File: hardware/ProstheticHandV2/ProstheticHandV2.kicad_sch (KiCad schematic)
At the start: 35 parts, among them J1 BATT_CONNECTOR, J2 EMG_SENSOR_01, J3 EMG_SENSOR_02, SW1 DIP_SWITCH, U1 LM7805_TO220

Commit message: Update work on schematic
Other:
- removed sheet Sheet2
- removed sheet Sheet3
- added sheet ProstheticHandV2_Sheet2 (ProstheticHandV2_Sheet2.kicad_sch)
- added sheet ProstheticHandV2_Sheet3 (ProstheticHandV2_Sheet3.kicad_sch)
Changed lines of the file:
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@@
+    )
+  )
+  (global_label "POT_01" (shape input) (at 40.64 68.58 180) (fields_autoplaced)
+    (effects (font (size 1.27 1.27)) (justify right))
+    (property "Intersheetrefs" "${INTERSHEET_REFS}" (at 30.7001 68.58 0)
+      (effects (font (size 1.27 1.27)) (justify right) hide)
     )
   )
@@
     )
   )
+  (global_label "BUTTON_01" (shape input) (at 45.72 88.9 180) (fields_autoplaced)
+    (effects (font (size 1.27 1.27)) (justify right))
+    (property "Intersheetrefs" "${INTERSHEET_REFS}" (at 32.1515 88.9 0)
+      (effects (font (size 1.27 1.27)) (justify right) hide)
+    )
+  )
   (global_label "DIP_SWITCH_02" (shape output) (at 43.18 165.1 180) (fields_autoplaced)
     (effects (font (size 1.27 1.27)) (justify right))
@@
     )
   )
+  (global_label "POT_02" (shape input) (at 43.18 73.66 180) (fields_autoplaced)
+    (effects (font (size 1.27 1.27)) (justify right))
+    (property "Intersheetrefs" "${INTERSHEET_REFS}" (at 33.2401 73.66 0)
+      (effects (font (size 1.27 1.27)) (justify right) hide)
+    )
+  )
   (global_label "DIP_SWITCH_03" (shape output) (at 43.18 170.18 180) (fields_autoplaced)
     (effects (font (size 1.27 1.27)) (justify right))
@@
     )
   )
+  (global_label "BUTTON_02" (shape input) (at 43.18 93.98 180) (fields_autoplaced)
+    (effects (font (size 1.27 1.27)) (justify right))
+    (property "Intersheetrefs" "${INTERSHEET_REFS}" (at 29.6115 93.98 0)
+      (effects (font (size 1.27 1.27)) (justify right) hide)
+    )
+  )
   (global_label "DIP_SWITCH_01" (shape input) (at 124.46 71.12 0) (fields_autoplaced)
     (effects (font (size 1.27 1.27)) (justify left))
@@
     (property "Intersheetrefs" "${INTERSHEET_REFS}" (at 141.536 58.42 0)
       (effects (font (size 1.27 1.27)) (justify left) hide)
+    )
+  )
+  (global_label "POT_03" (shape input) (at 43.18 81.28 180) (fields_autoplaced)
+    (effects (font (size 1.27 1.27)) (justify right))
+    (property "Intersheetrefs" "${INTERSHEET_REFS}" (at 33.2401 81.28 0)
+      (effects (font (size 1.27 1.27)) (justify right) hide)
     )
   )
@@
     )
   )
-  (sheet (at 0 457.2) (size 297.18 210.82) (fields_autoplaced)
+  (sheet (at 2.54 228.6) (size 302.26 193.04) (fields_autoplaced)
     (stroke (width 0.1524) (type solid))
     (fill (color 0 0 0 0.0000))
-    (property "Sheetname" "Sheet3" (at 0 456.4884 0)
+    (property "Sheetname" "ProstheticHandV2_Sheet2" (at 2.54 227.8884 0)
       (effects (font (size 1.27 1.27)) (justify left bottom))
     )
-    (property "Sheetfile" "untitled.kicad_sch" (at 0 668.6046 0)
+    (property "Sheetfile" "ProstheticHandV2_Sheet2.kicad_sch" (at 2.54 422.2246 0)
       (effects (font (size 1.27 1.27)) (justify left top))
     )
@@
     )
   )
-  (sheet (at 0 223.52) (size 297.18 210.82) (fields_autoplaced)
+  (sheet (at 5.08 439.42) (size 299.72 180.34) (fields_autoplaced)
     (stroke (width 0.1524) (type solid))
     (fill (color 0 0 0 0.0000))
-    (property "Sheetname" "Sheet2" (at 0 222.8084 0)
+    (property "Sheetname" "ProstheticHandV2_Sheet3" (at 5.08 438.7084 0)
       (effects (font (size 1.27 1.27)) (justify left bottom))
     )
-    (property "Sheetfile" "untitled.kicad_sch" (at 0 434.9246 0)
+    (property "Sheetfile" "ProstheticHandV2_Sheet3.kicad_sch" (at 5.08 620.3446 0)
       (effects (font (size 1.27 1.27)) (justify left top))
     )
     (instances
       (project "ProstheticHandV2"
-        (path "/4b4c4f07-d40b-46d6-800c-cabc6090ace0" (page "2"))
-      )
-    )
+        (path "/4b4c4f07-d40b-46d6-800c-cabc6090ace0" (page "3"))
+      )
+    )

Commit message: Started working on PCB
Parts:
- A1: footprint (none) -> FootprintLibrary:ESP32S3_DevModule
- C1, C2, C5, C6: footprint (none) -> Capacitor_THT:C_Disc_D3.8mm_W2.6mm_P2.50mm
- C3, C4: footprint (none) -> Capacitor_THT:CP_Radial_D8.0mm_P3.50mm
- D1: footprint (none) -> Diode_THT:D_DO-15_P12.70mm_Horizontal
- D2, D3: footprint (none) -> LED_THT:LED_D5.0mm
- D4, D5: footprint (none) -> Diode_THT:D_T-1_P5.08mm_Horizontal
- D6: value GREEN -> LED GREEN; footprint (none) -> LED_THT:LED_D5.0mm
- J1, J2, J3: footprint (none) -> Connector_JST:JST_XA_B02B-XASK-1-A_1x02_P2.50mm_Vertical
- R1, R2, R3, R4, R5, R6, R7, R8, R9: footprint (none) -> Resistor_THT:R_Axial_DIN0207_L6.3mm_D2.5mm_P7.62mm_Horizontal
- SW1: footprint (none) -> Button_Switch_THT:SW_DIP_SPSTx04_Slide_9.78x12.34mm_W7.62mm_P2.54mm
- TP1, TP2, TP3, TP4, TP5, TP6, TP7, TP8: footprint (none) -> TestPoint:TestPoint_Pad_D2.5mm
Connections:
- net +3V3: now also A1.1 (3v3), A1.2 (3v3); no longer A1. (TX)
- net +5V: now also A1.21 (5v); no longer A1. (TX)
- net BATT_SENSE: now also A1.20 (14)
- net BUTTON_01: now also A1.40 (2)
- net BUTTON_02: now also A1.41 (1)
- net DEBUG_LED_01: now also A1.34 (37)
- net DEBUG_LED_02: now also A1.35 (38)
- net DIP_SWITCH_00: now also A1.39 (42)
- net DIP_SWITCH_01: now also A1.38 (41)
- net DIP_SWITCH_02: now also A1.37 (40)
- net DIP_SWITCH_03: now also A1.36 (39)
- net EMG_SENSOR_01: now also A1.10 (17)
- net EMG_SENSOR_02: now also A1.11 (18)
- net GND: now also A1.22 (GND), A1.23 (GND), A1.24 (GND), A1.44 (GND); no longer A1. (TX)
- net POT_01: now also A1.16 (10)
- net POT_02: now also A1.17 (11)
- net POT_03: now also A1.18 (12)
- new net SERVO_CONTROL_01: A1.4
- new net SERVO_CONTROL_02: A1.5
- new net SERVO_CONTROL_03: A1.6
- new net SERVO_CURR_01: A1.7
- new net SERVO_CURR_02: A1.8 (15)
- new net SERVO_CURR_03: A1.9 (16)

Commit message: Finalize PCB design for china
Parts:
- added TP3: TP_GND, TestPoint:TestPoint_Pad_D2.5mm, symbol Connector:TestPoint
- J1, J2, J3: footprint Connector_JST:JST_XA_B02B-XASK-1-A_1x02_P2.50mm_Vertical -> Connector_JST:JST_XA_B02B-XASK-1_1x02_P2.50mm_Vertical
- renumbered C3 to C1, C4 to C3, C1 to C4, D6 to D2, D4 to D3, D5 to D4, D2 to D5, D3 to D6, R9 to R2, R2 to R3, R5 to R4, R6 to R5, R7 to R6, R8 to R7, R3 to R8, R4 to R9, TP5 to TP4, TP7 to TP5, TP8 to TP7, TP3 to TP8, TP4 to TP9
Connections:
- net BUTTON_01: now also A1.41 (1); no longer A1.40 (2)
- net BUTTON_02: now also A1.40 (2); no longer A1.41 (1)
- net EMG_SENSOR_01: now also A1.11 (18); no longer A1.10 (17)
- net EMG_SENSOR_02: now also A1.10 (17); no longer A1.11 (18)
- net GND: now also TP3.1

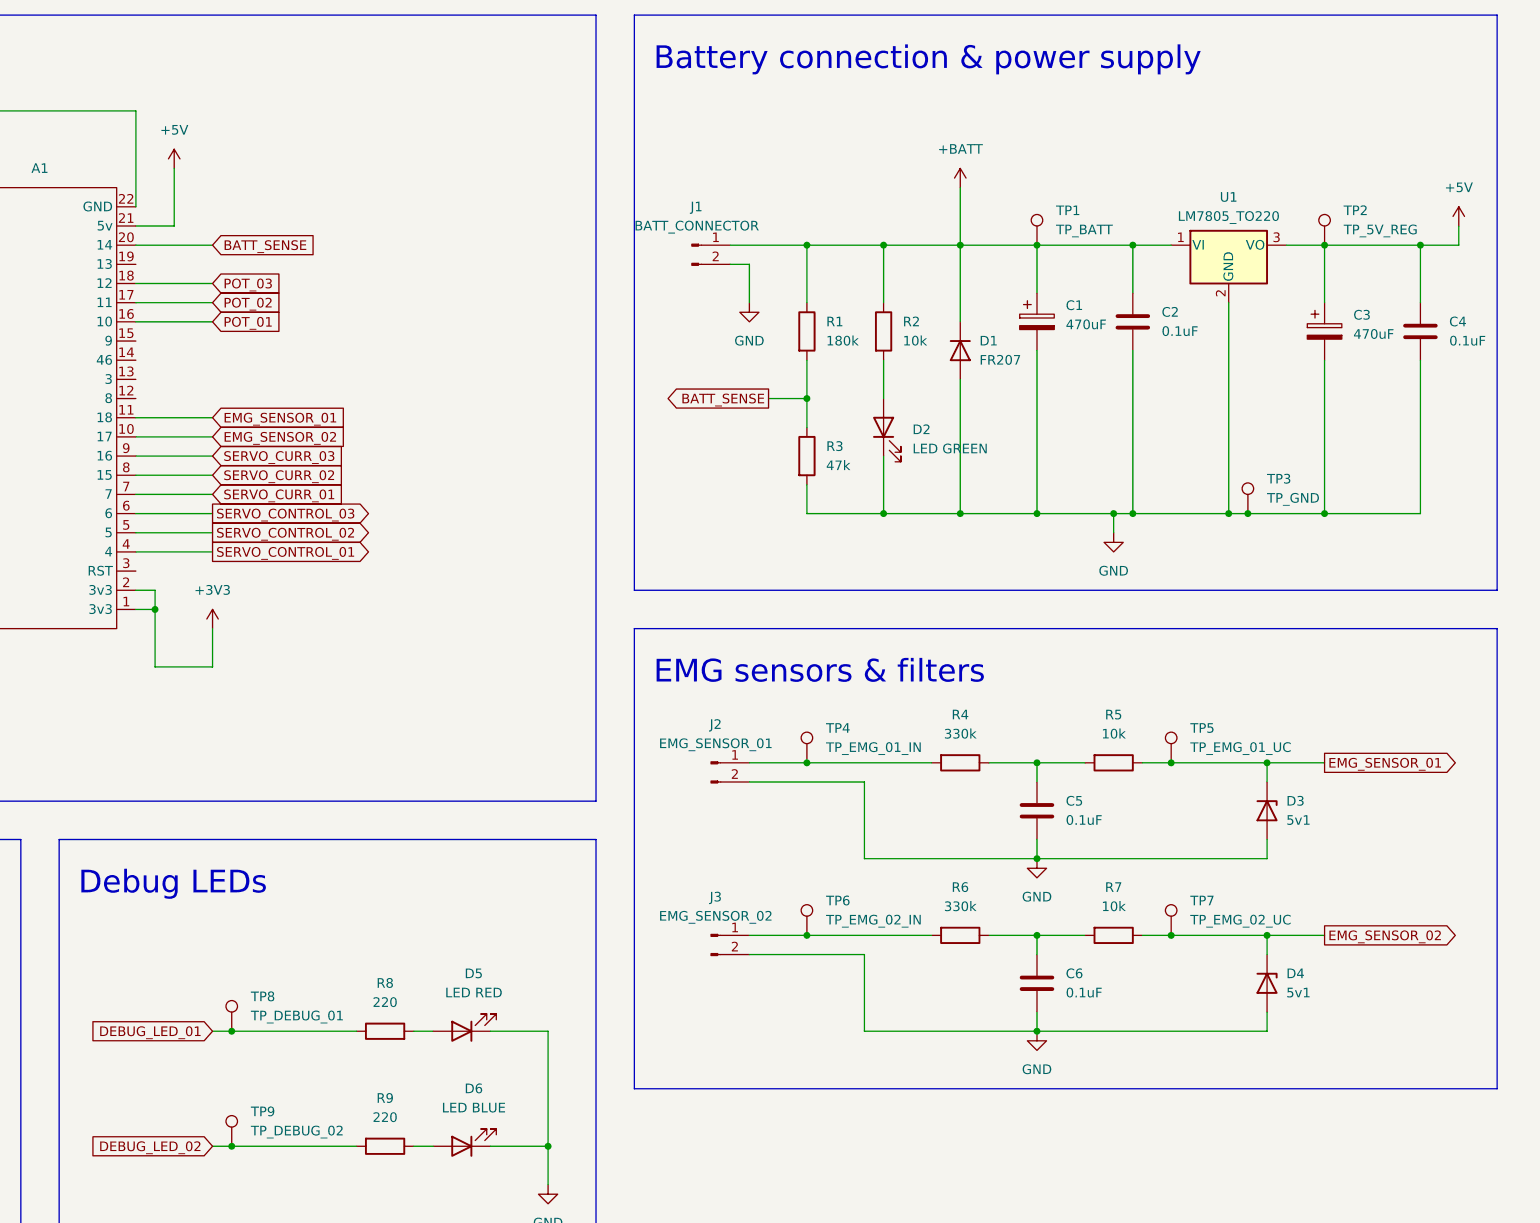
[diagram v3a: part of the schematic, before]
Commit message: Update PCB, sent to JLCPCB
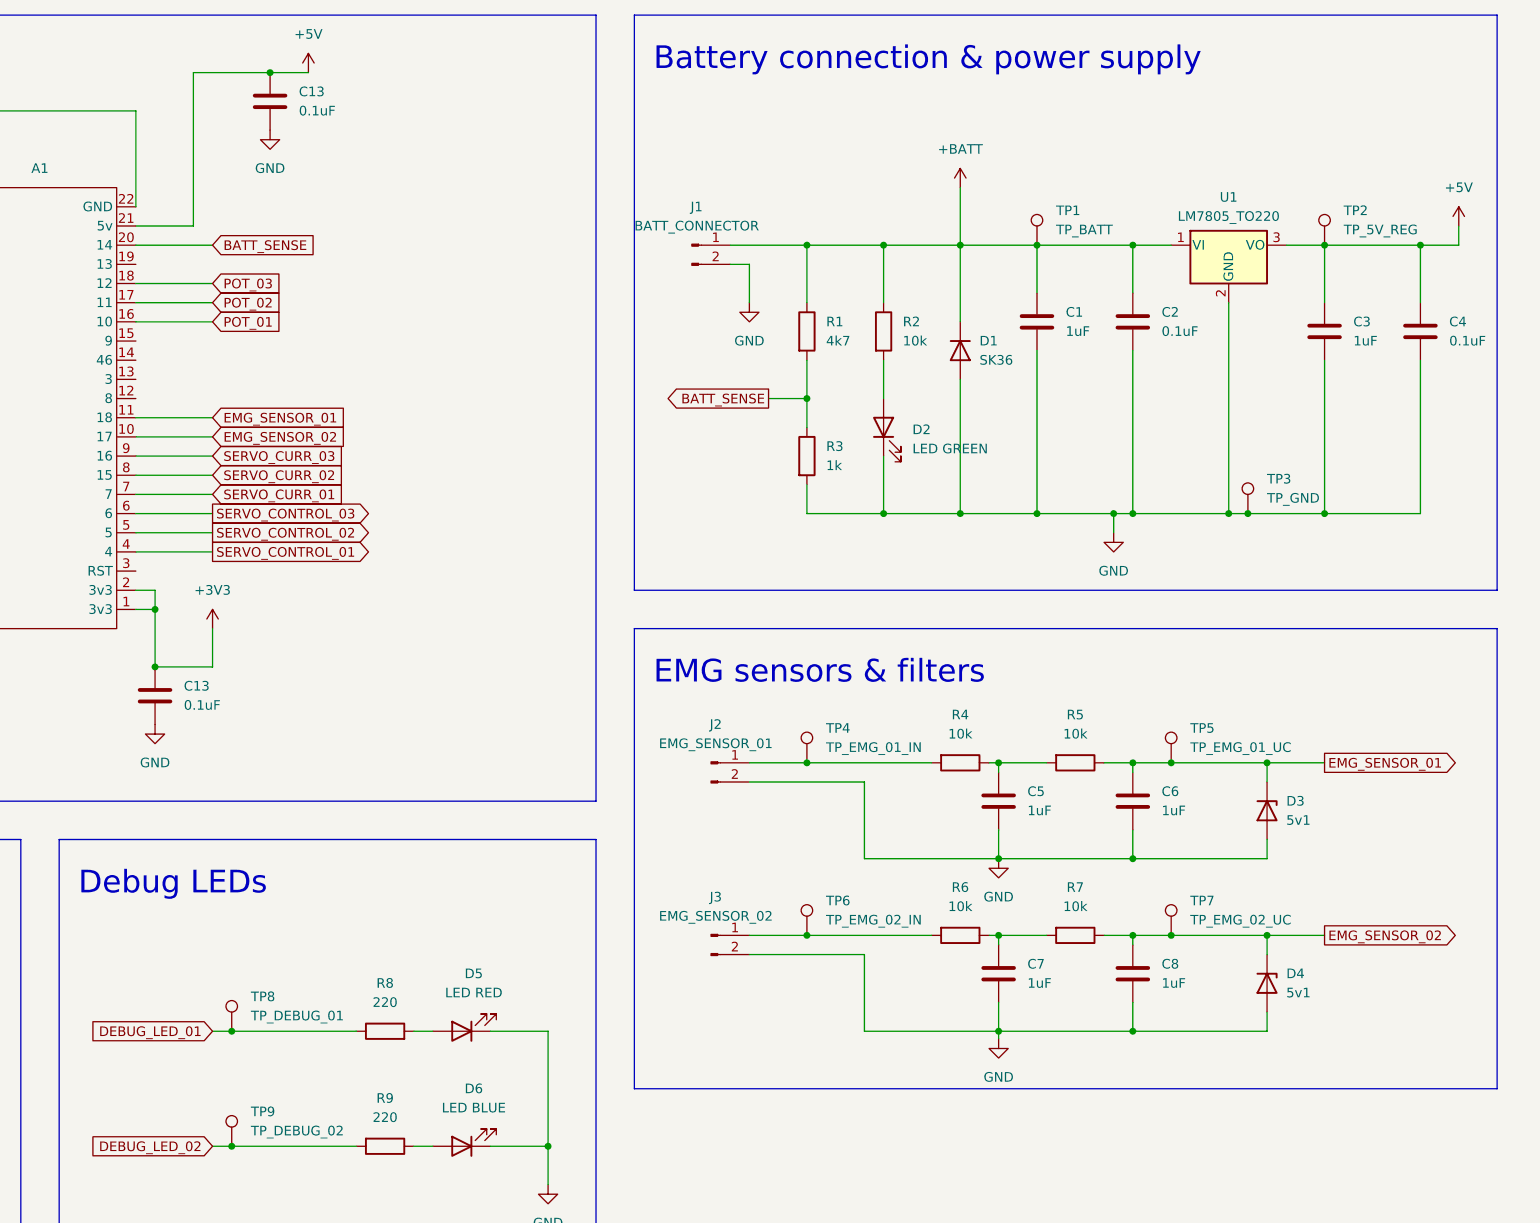
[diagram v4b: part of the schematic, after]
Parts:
- removed C1, C3: 470uF, Capacitor_THT:CP_Radial_D8.0mm_P3.50mm, symbol Device:C_Polarized
- added C1, C3, C7, C8: 1uF, Capacitor_SMD:C_1206_3216Metric, symbol Device:C
- added C13 (x2): 0.1uF, Capacitor_SMD:C_1206_3216Metric, symbol Device:C
- C2, C4: footprint Capacitor_THT:C_Disc_D3.8mm_W2.6mm_P2.50mm -> Capacitor_SMD:C_1206_3216Metric
- C5, C6: value 0.1uF -> 1uF; footprint Capacitor_THT:C_Disc_D3.8mm_W2.6mm_P2.50mm -> Capacitor_SMD:C_1206_3216Metric
- D1: value FR207 -> SK36; footprint Diode_THT:D_DO-15_P12.70mm_Horizontal -> Diode_SMD:D_SMC
- R1: value 180k -> 4k7; footprint Resistor_THT:R_Axial_DIN0207_L6.3mm_D2.5mm_P7.62mm_Horizontal -> Resistor_SMD:R_1206_3216Metric
- R2, R5, R7, R8, R9: footprint Resistor_THT:R_Axial_DIN0207_L6.3mm_D2.5mm_P7.62mm_Horizontal -> Resistor_SMD:R_1206_3216Metric
- R3: value 47k -> 1k; footprint Resistor_THT:R_Axial_DIN0207_L6.3mm_D2.5mm_P7.62mm_Horizontal -> Resistor_SMD:R_1206_3216Metric
- R4, R6: value 330k -> 10k; footprint Resistor_THT:R_Axial_DIN0207_L6.3mm_D2.5mm_P7.62mm_Horizontal -> Resistor_SMD:R_1206_3216Metric
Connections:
- net +3V3: now also C13.1
- net +5V: now also C13.1, C3.1
- net +BATT: now also C1.1
- net EMG_SENSOR_01: now also C6.1
- net EMG_SENSOR_02: now also C8.1
- net GND: now also C1.2, C13.2, C13.2, C3.2, C7.2, C8.2
- net at R6.1, R7.2: now also C7.1; no longer C6.1
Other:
- moved on the sheet: C5, R5
